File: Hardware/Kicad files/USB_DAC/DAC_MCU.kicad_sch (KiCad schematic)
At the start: 42 parts, among them J6 Conn_ARM_JTAG_SWD_10, U1 USB3300-EZK, U2 STM32H723ZGTx, Y1 Crystal_48MHz, Y2 Crystal_Small

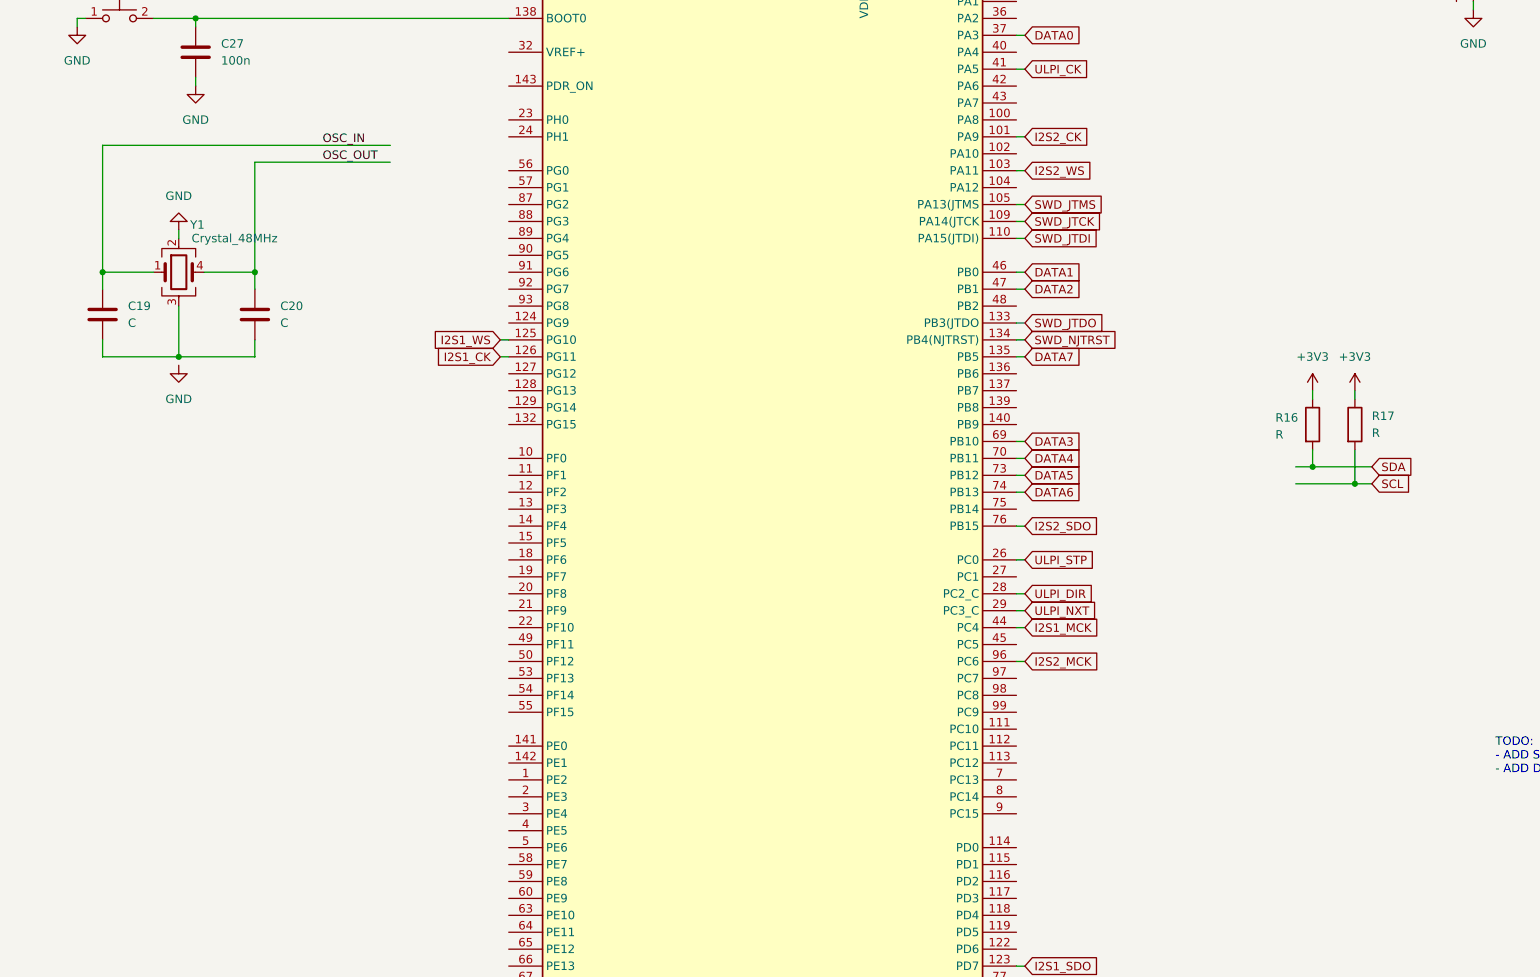
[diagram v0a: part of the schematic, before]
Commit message: added STM code files and modified PCB
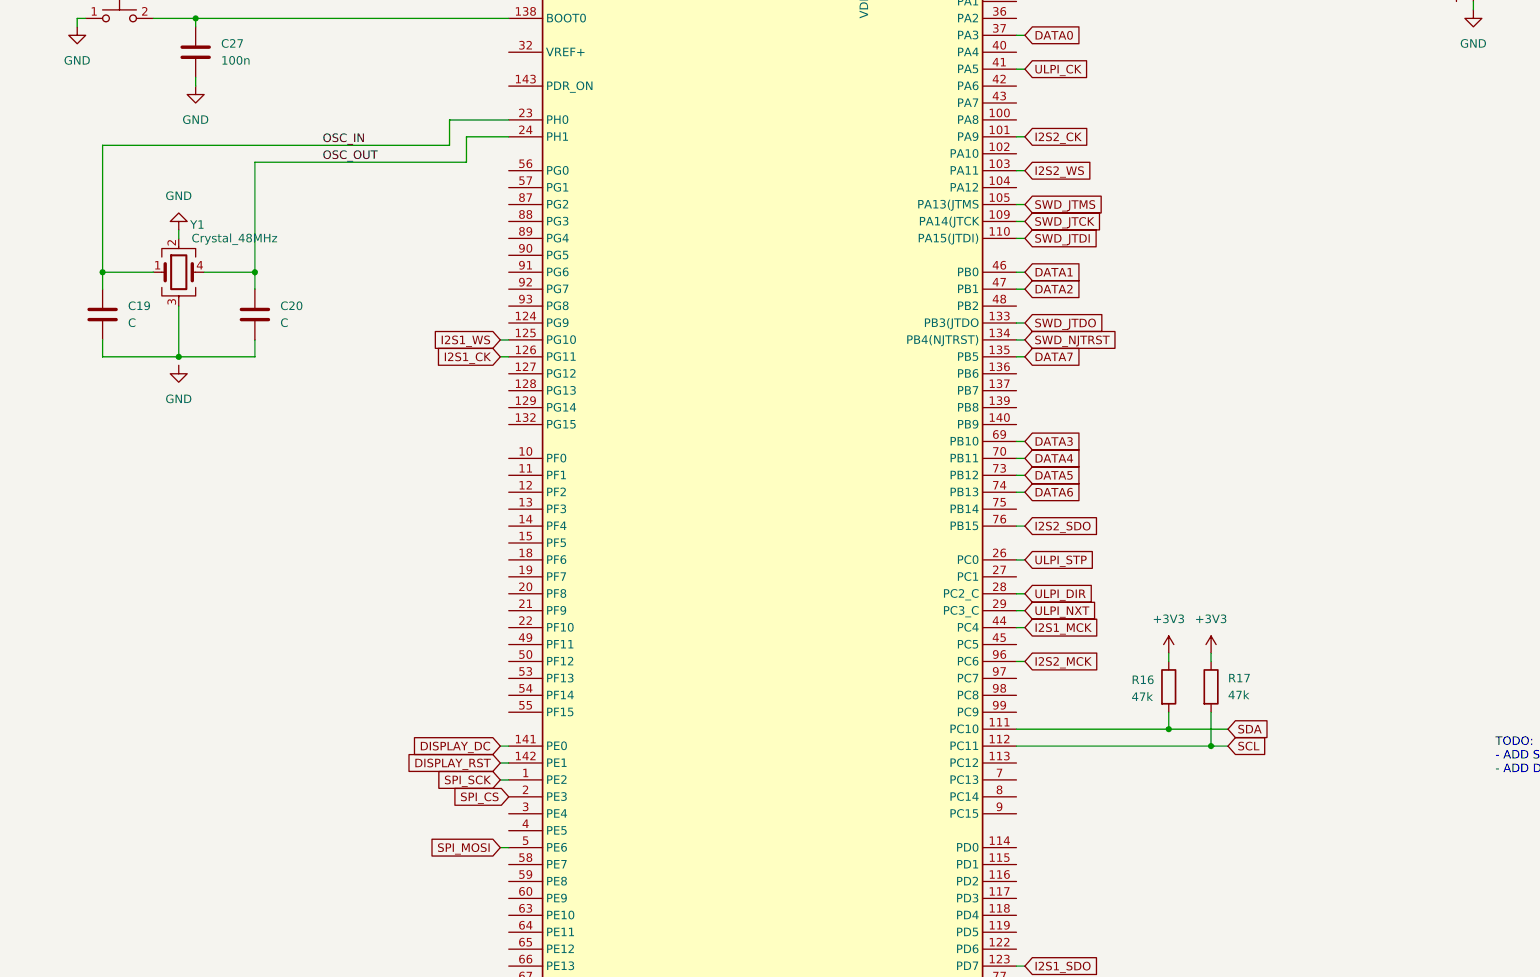
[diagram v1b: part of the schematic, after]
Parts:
- R16, R17: value R -> 47k
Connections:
- net OSC_IN: now also U2.23 (PH0)
- net OSC_OUT: now also U2.24 (PH1)
- net SCL: now also U2.112 (PC11)
- net SDA: now also U2.111 (PC10)
- net SPI_SCK: now reaches U2.1 (PE2)
- net DISPLAY_DC: now reaches U2.141 (PE0)
- net DISPLAY_RST: now reaches U2.142 (PE1)
- net SPI_CS: now reaches U2.2 (PE3)
- net SPI_MOSI: now reaches U2.5 (PE6)
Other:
- moved on the sheet: R16, R17

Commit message: Updated PCB and schematics
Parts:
- removed Y1: Crystal_48MHz, symbol Device:Crystal_GND23
- added C46, C47, C48: 1u, Capacitor_SMD:C_0603_1608Metric, symbol Device:C
- added R27: 10k, Resistor_SMD:R_0603_1608Metric, symbol Device:R
- added U8: TPS7A2033PDBVR, TPS7A2033PDBVR:SOT95P280X145-5N, symbol TPS7A2033PDBVR:TPS7A2033PDBVR
- added U9: MAX6816EUS_T, MAX6816EUS_T:SOT192P237X122-4N, symbol MAX6816EUS_T:MAX6816EUS_T
- added Y1, Y4: C5S-20.000-12-3030-X-R, C5S-20.000-12-3030-X-R:XTAL_C5S-20.000-12-3030-X-R, symbol C5S-20.000-12-3030-X-R:C5S-20.000-12-3030-X-R
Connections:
- net +3V3: now also J6.1 (VTref), C46.1, C48.1, R27.2, U8.5 (OUT), U9.4 (VCC)
- net ACT_LED: now also U2.8 (PC14)
- net DISPLAY_DC: now also U2.142 (PE1); no longer U2.141 (PE0)
- net DISPLAY_RST: now also U2.141 (PE0); no longer U2.142 (PE1)
- net ERR_LED: now also U2.9 (PC15)
- net GND: now also C19.2, C20.2, C46.2, C47.2, C48.2, U8.2 (GND), U9.1 (GND), Y1.2 (GND), Y1.4 (GND), Y4.2 (GND), Y4.4 (GND)
- net OSC_IN: now also Y1.1
- net OSC_OUT: now also Y1.3
- net PHY_OSC_IN: now also Y4.3
- net PHY_OSC_OUT: now also Y4.1
- new net +5V: C47.1, U8.1 (IN), U8.3 (EN)
- new net BTN: R27.1, U9.2 (IN)
- new net BTN_MCU: U9.3 (OUT)
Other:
- note removed: "TODO: - ADD SPI FOR DISPLAY - ADD DEBUG LEDSz"
- company: (none) -> Linus Fridlund
- title: (none) -> MCU Sheet
- moved on the sheet: D1, D2, J6, R6, R7
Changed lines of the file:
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@@
 	(generator_version "9.0")
 	(paper "A3")
+	(title_block
+		(title "MCU Sheet")
+		(rev "1.0")
+		(company "Linus Fridlund")
+	)

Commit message: Updated PCB and schematics
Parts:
- added C49, C50, C51, C52: 1u, Capacitor_SMD:C_0603_1608Metric, symbol Device:C
- added R28: 10k, Resistor_SMD:R_0603_1608Metric, symbol Device:R
- added U10: LM1117MP-5.0, Package_TO_SOT_SMD:SOT-223-3_TabPin2, symbol Regulator_Linear:LM1117MP-5.0
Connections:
- net +3V3: now also R28.2
- net +5V: now also C51.1, C52.1, U10.2 (VO)
- net BTN_MCU: now also U2.35 (PA1)
- net GND: now also C49.2, C50.2, C51.2, C52.2, U10.1 (GND)
- net at C26.1, RST1.2 (D), U2.25 (NRST): now also R28.1
- net BTN_LED: now reaches U2.36 (PA2)
- new net DC_IN: C49.1, C50.1, U10.3 (VI)
